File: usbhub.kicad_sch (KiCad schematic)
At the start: 22 parts

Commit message: start rework of baseboard.
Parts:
- gave numbers to parts that had none: 22

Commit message: replace display with better module, start layout parts on pcb.
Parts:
- C41, C43, C45, C46: footprint eduboardv2:C0402 -> Capacitor_SMD:C_0402_1005Metric_Pad0.74x0.62mm_HandSolder
- C42, C44: footprint C0402 -> Capacitor_SMD:C_0402_1005Metric_Pad0.74x0.62mm_HandSolder
- IC10: footprint QFN-36_L6.0-W6.0-P0.50-BL-EP -> EduboardV2_kicadlib:TQFN-36_L6.0-W6.0-P0.50-BL-EP3.7
- R60, R61, R62, R63, R64, R65, R66, R67, R68, R69, R70, R71, R72, R73: footprint R0402 -> Resistor_SMD:R_0402_1005Metric_Pad0.72x0.64mm_HandSolder
- X15: footprint OSC-SMD_4P-L3.2-W2.5-BL -> EduboardV2_kicadlib:OSC-SMD_4P-L3.2-W2.5-BL
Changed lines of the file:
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@@
       (effects (font (size 1.27 1.27)) (justify left))
     )
-    (property "Footprint" "eduboardv2:C0402" (at 185.42 86.36 0)
+    (property "Footprint" "Capacitor_SMD:C_0402_1005Metric_Pad0.74x0.62mm_HandSolder" (at 185.42 86.36 0)
       (effects (font (size 1.27 1.27)) hide)
     )
@@
       (effects (font (size 1.27 1.27)) (justify right))
     )
-    (property "Footprint" "R0402" (at 205.74 85.09 0)
+    (property "Footprint" "Resistor_SMD:R_0402_1005Metric_Pad0.72x0.64mm_HandSolder" (at 205.74 85.09 0)
       (effects (font (size 1.27 1.27)) hide)
     )
@@
       (effects (font (size 1.27 1.27)) (justify right))
     )
-    (property "Footprint" "R0402" (at 209.55 118.11 0)
+    (property "Footprint" "Resistor_SMD:R_0402_1005Metric_Pad0.72x0.64mm_HandSolder" (at 209.55 118.11 0)
       (effects (font (size 1.27 1.27)) hide)
     )
@@
       (effects (font (size 1.27 1.27)) (justify left))
     )
-    (property "Footprint" "eduboardv2:C0402" (at 224.79 110.49 0)
+    (property "Footprint" "Capacitor_SMD:C_0402_1005Metric_Pad0.74x0.62mm_HandSolder" (at 224.79 110.49 0)
       (effects (font (size 1.27 1.27)) hide)
     )
@@
       (effects (font (size 1.27 1.27)) (justify left))
     )
-    (property "Footprint" "R0402" (at 231.14 116.84 0)
+    (property "Footprint" "Resistor_SMD:R_0402_1005Metric_Pad0.72x0.64mm_HandSolder" (at 231.14 116.84 0)
       (effects (font (size 1.27 1.27)) hide)
     )
@@
       (effects (font (size 1.27 1.27)) (justify right))
     )
-    (property "Footprint" "R0402" (at 257.81 96.52 0)
+    (property "Footprint" "Resistor_SMD:R_0402_1005Metric_Pad0.72x0.64mm_HandSolder" (at 257.81 96.52 0)
       (effects (font (size 1.27 1.27)) hide)
     )
@@
       (effects (font (size 1.27 1.27)) (justify left))
     )
-    (property "Footprint" "R0402" (at 19.05 68.58 0)
+    (property "Footprint" "Resistor_SMD:R_0402_1005Metric_Pad0.72x0.64mm_HandSolder" (at 19.05 68.58 0)
       (effects (font (size 1.27 1.27)) hide)
     )
@@
       (effects (font (size 1.27 1.27)) (justify right))
     )
-    (property "Footprint" "R0402" (at 227.33 113.03 0)
+    (property "Footprint" "Resistor_SMD:R_0402_1005Metric_Pad0.72x0.64mm_HandSolder" (at 227.33 113.03 0)
       (effects (font (size 1.27 1.27)) hide)
     )
@@
       (effects (font (size 1.27 1.27)))
     )
-    (property "Footprint" "C0402" (at 209.55 66.04 0)
+    (property "Footprint" "Capacitor_SMD:C_0402_1005Metric_Pad0.74x0.62mm_HandSolder" (at 209.55 66.04 0)
       (effects (font (size 1.27 1.27)) hide)
     )
@@
       (effects (font (size 1.27 1.27)))
     )
-    (property "Footprint" "OSC-SMD_4P-L3.2-W2.5-BL" (at 195.58 71.12 0)
+    (property "Footprint" "EduboardV2_kicadlib:OSC-SMD_4P-L3.2-W2.5-BL" (at 195.58 71.12 0)
       (effects (font (size 1.27 1.27)) hide)
     )
@@
       (effects (font (size 1.27 1.27)))
     )
-    (property "Footprint" "C0402" (at 181.61 71.12 0)
+    (property "Footprint" "Capacitor_SMD:C_0402_1005Metric_Pad0.74x0.62mm_HandSolder" (at 181.61 71.12 0)
       (effects (font (size 1.27 1.27)) hide)
     )
@@
       (effects (font (size 1.27 1.27)) (justify left))
     )
-    (property "Footprint" "R0402" (at 44.45 68.58 0)
+    (property "Footprint" "Resistor_SMD:R_0402_1005Metric_Pad0.72x0.64mm_HandSolder" (at 44.45 68.58 0)
       (effects (font (size 1.27 1.27)) hide)
     )
@@
       (effects (font (size 1.27 1.27)) (justify left))
     )
-    (property "Footprint" "R0402" (at 231.14 106.68 0)
+    (property "Footprint" "Resistor_SMD:R_0402_1005Metric_Pad0.72x0.64mm_HandSolder" (at 231.14 106.68 0)
       (effects (font (size 1.27 1.27)) hide)
     )
@@
       (effects (font (size 1.27 1.27)) (justify right))
     )
-    (property "Footprint" "R0402" (at 223.52 92.71 0)
+    (property "Footprint" "Resistor_SMD:R_0402_1005Metric_Pad0.72x0.64mm_HandSolder" (at 223.52 92.71 0)
       (effects (font (size 1.27 1.27)) hide)
     )
@@
       (effects (font (size 1.27 1.27)) (justify left))
     )
-    (property "Footprint" "R0402" (at 231.14 93.98 0)
+    (property "Footprint" "Resistor_SMD:R_0402_1005Metric_Pad0.72x0.64mm_HandSolder" (at 231.14 93.98 0)
       (effects (font (size 1.27 1.27)) hide)
     )
@@
       (effects (font (size 1.27 1.27)) (justify left))
     )
-    (property "Footprint" "R0402" (at 36.83 68.58 0)
+    (property "Footprint" "Resistor_SMD:R_0402_1005Metric_Pad0.72x0.64mm_HandSolder" (at 36.83 68.58 0)
       (effects (font (size 1.27 1.27)) hide)
     )
@@
       (effects (font (size 1.27 1.27)) (justify right))
     )
-    (property "Footprint" "R0402" (at 218.44 113.03 0)
+    (property "Footprint" "Resistor_SMD:R_0402_1005Metric_Pad0.72x0.64mm_HandSolder" (at 218.44 113.03 0)
       (effects (font (size 1.27 1.27)) hide)
     )
@@
       (effects (font (size 1.27 1.27)) (justify left))
     )
-    (property "Footprint" "eduboardv2:C0402" (at 35.56 135.89 0)
+    (property "Footprint" "Capacitor_SMD:C_0402_1005Metric_Pad0.74x0.62mm_HandSolder" (at 35.56 135.89 0)
       (effects (font (size 1.27 1.27)) hide)
     )
@@
       (effects (font (size 1.27 1.27)) (justify left))
     )
-    (property "Footprint" "eduboardv2:C0402" (at 242.57 107.95 0)
+    (property "Footprint" "Capacitor_SMD:C_0402_1005Metric_Pad0.74x0.62mm_HandSolder" (at 242.57 107.95 0)
       (effects (font (size 1.27 1.27)) hide)
     )
@@
       (effects (font (size 1.27 1.27)))
     )
-    (property "Footprint" "R0402" (at 193.04 80.01 0)
+    (property "Footprint" "Resistor_SMD:R_0402_1005Metric_Pad0.72x0.64mm_HandSolder" (at 193.04 80.01 0)
       (effects (font (size 1.27 1.27)) hide)
     )
@@
       (effects (font (size 1.27 1.27)) (justify left))
     )
-    (property "Footprint" "R0402" (at 27.94 68.58 0)
+    (property "Footprint" "Resistor_SMD:R_0402_1005Metric_Pad0.72x0.64mm_HandSolder" (at 27.94 68.58 0)
       (effects (font (size 1.27 1.27)) hide)
     )
@@
       (effects (font (size 1.27 1.27)))
     )
-    (property "Footprint" "QFN-36_L6.0-W6.0-P0.50-BL-EP" (at 124.46 128.27 0)
-      (effects (font (size 1.27 1.27)) hide)
-    )
+    (property "Footprint" "EduboardV2_kicadlib:TQFN-36_L6.0-W6.0-P0.50-BL-EP3.7" (at 124.46 128.27 0)
+      (effects (font (size 1.27 1.27)) hide)
+    )

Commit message: Layout of parts done. Started laying tracks
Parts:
- added C25 (x6): 100nF, Capacitor_SMD:C_0402_1005Metric_Pad0.74x0.62mm_HandSolder, symbol eduboardv2:CL05B104KB54PNC
- added C26 (x6): 1uF, Capacitor_SMD:C_0402_1005Metric_Pad0.74x0.62mm_HandSolder, symbol eduboardv2:CL05A105KA5NQNC
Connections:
- net +3.3V: now also C25.2, C25.2, C25.2, C25.2, C25.2, C25.2, C26.2, C26.2, C26.2, C26.2, C26.2, C26.2
- net GND: now also C25.1, C25.1, C25.1, C25.1, C25.1, C25.1, C26.1, C26.1, C26.1, C26.1, C26.1, C26.1

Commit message: fix some wrong jlcpcb part numbers
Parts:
- R64: LCSC Part C26083 -> C25741
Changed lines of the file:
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@@
       (effects (font (size 1.27 1.27)) hide)
     )
-    (property "LCSC Part" "C26083" (at 193.04 87.63 0)
+    (property "LCSC Part" "C25741" (at 193.04 87.63 0)
       (effects (font (size 1.27 1.27)) hide)
     )

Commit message: add some part alternatives and create production data
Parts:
- X15: Alternative (none) -> C2149060
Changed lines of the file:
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@@
+      (effects (font (size 1.27 1.27)) hide)
+    )
+    (property "Alternative" "C2149060" (at 195.58 60.96 0)
       (effects (font (size 1.27 1.27)) hide)
     )

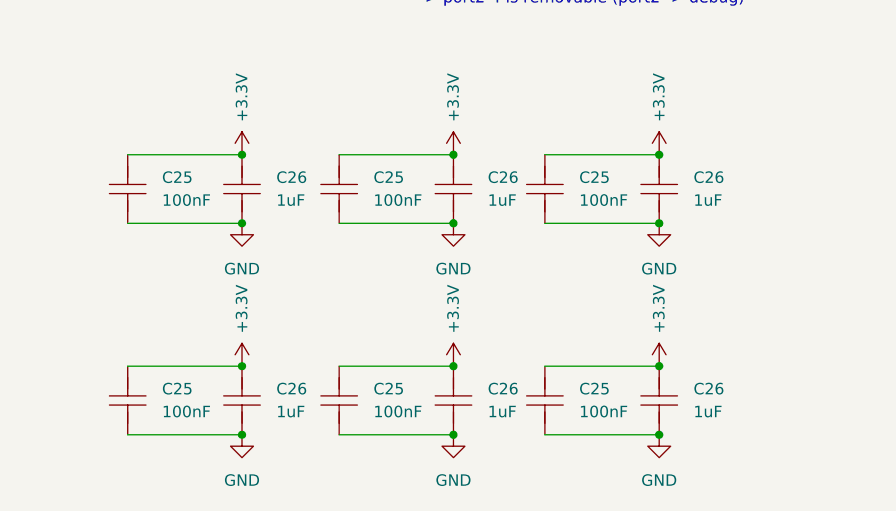
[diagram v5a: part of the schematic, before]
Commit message: migrate to kicad version 8. Add some alternative part numbers
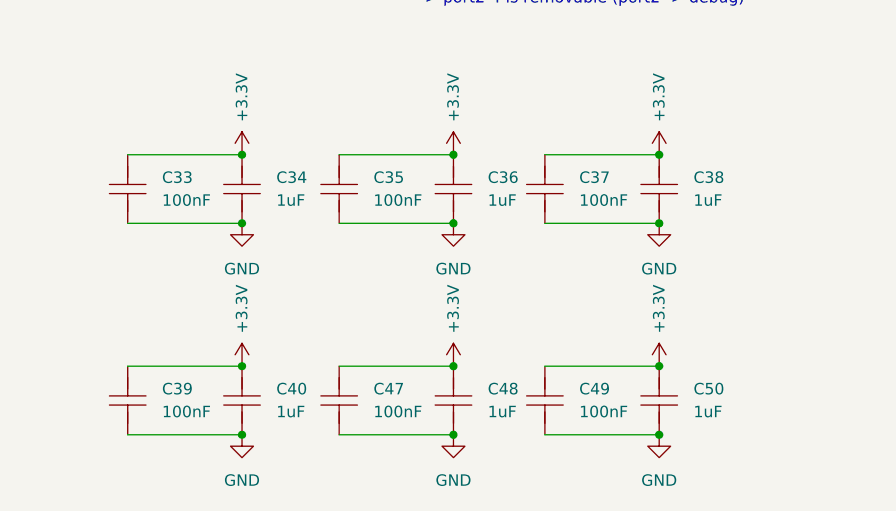
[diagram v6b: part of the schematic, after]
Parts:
- renumbered C25 to C33, C26 to C34, C25 to C35, C26 to C36, C25 to C37, C26 to C38, C25 to C39, C26 to C40, C25 to C47, C26 to C48, C25 to C49, C26 to C50
